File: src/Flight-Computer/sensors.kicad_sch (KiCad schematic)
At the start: 36 parts, among them P4 440054-3, P5 440054-3, P6 440054-3, P7 440054-3, Q1 QS5U17TR, Q2 QS5U17TR, Q3 QS5U17TR, Q4 QS5U17TR, U3 BMI323, U4 MAX-8C-0-10, U5 BMP390

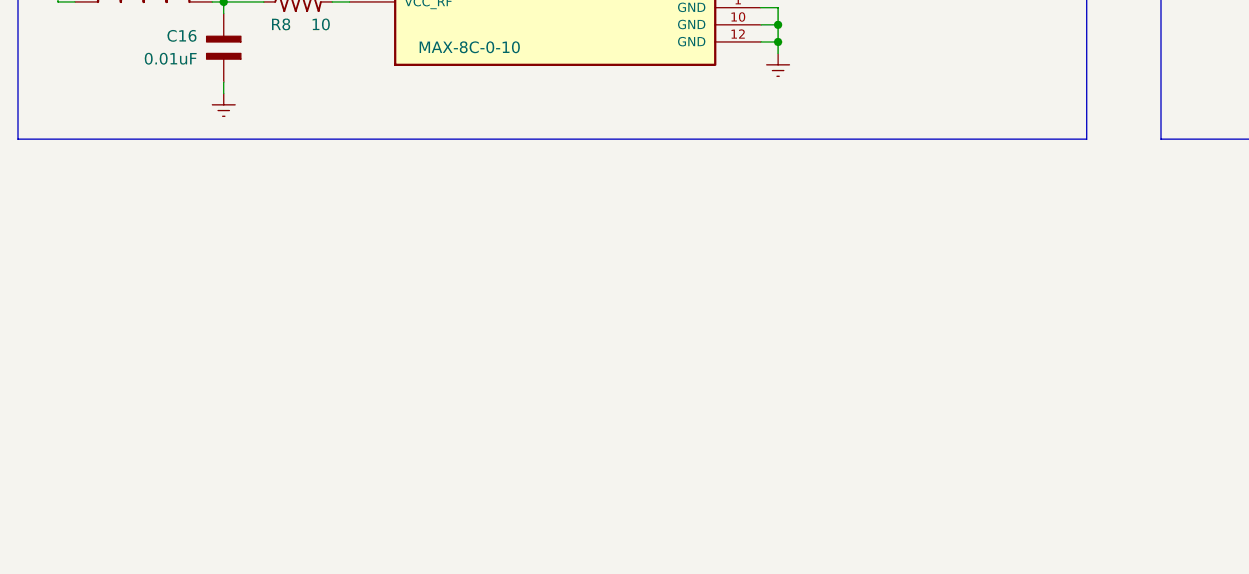
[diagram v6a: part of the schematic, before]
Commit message: implemented magnetometer in schematic
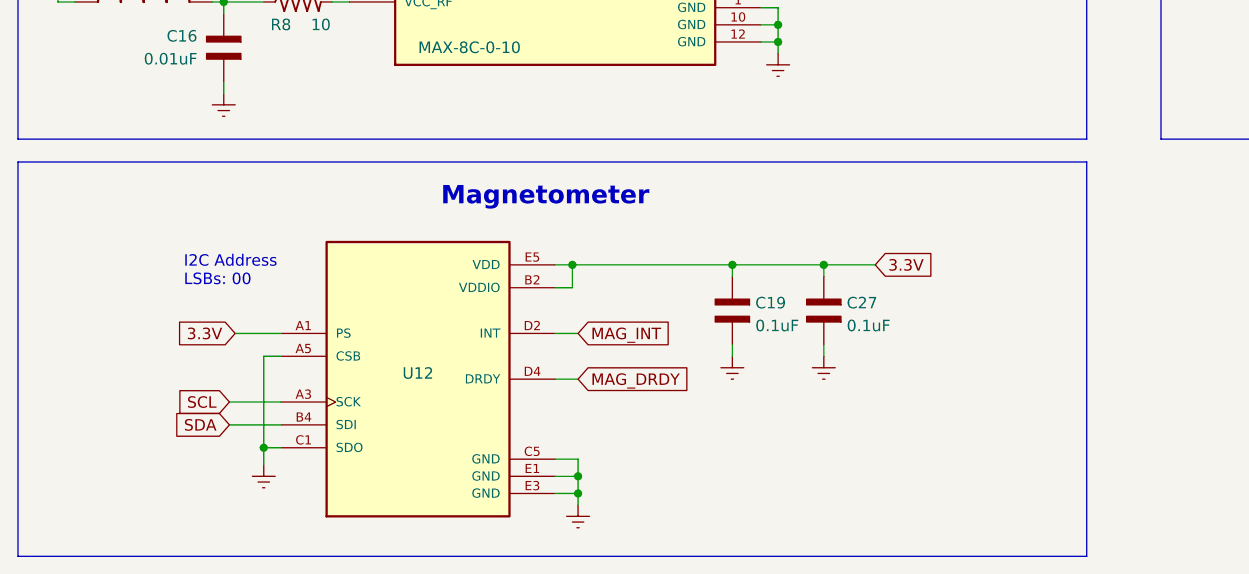
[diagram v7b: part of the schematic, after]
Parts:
- added C19, C27: 0.1uF, Flight-Computer:CAP_0603, symbol Flight-Computer:CAP_0603
- added U12: BMM150, Flight-Computer:BMM150, symbol Flight-Computer:BMM150
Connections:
- net 3.3V: now also C19.1, C27.1, U12.A1 (PS), U12.B2 (VDDIO), U12.E5 (VDD)
- net Earth: now also C19.2, C27.2, U12.A5 (CSB), U12.C1 (SDO), U12.C5 (GND), U12.E1 (GND), U12.E3 (GND)
- net SCL: now also U12.A3 (SCK)
- net SDA: now also U12.B4 (SDI)
- new net MAG_DRDY: U12.D4 (DRDY)
- new net MAG_INT: U12.D2 (INT)
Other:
- note added: "I2C Address LSBs: 00"
- note added: "Magnetometer"

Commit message: matched footprints to symbols
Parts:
- Q1, Q2, Q3, Q4: footprint Engine-Controller:QS5U17TR -> Flight-Computer:QS5U17TR
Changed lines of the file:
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@@
     (pin "1")
   )
-  (symbol (lib_name "QS5U17TR_1") (lib_id "Flight-Computer:QS5U17TR") (at 182.88 104.775 0) (unit 1)
+  (symbol (lib_id "Flight-Computer:QS5U17TR") (at 182.88 104.775 0) (unit 1)
     (in_bom yes) (on_board yes) (fields_autoplaced)
     (property "Reference" "Q1" (id 0) (at 188.087 105.2088 0)
@@
       (effects (font (size 1.27 1.27)) (justify left) hide)
     )
-    (property "Footprint" "Engine-Controller:QS5U17TR" (id 2) (at 184.785 120.65 0)
+    (property "Footprint" "Flight-Computer:QS5U17TR" (id 2) (at 184.785 120.65 0)
       (effects (font (size 1.27 1.27) italic) (justify left) hide)
     )
@@
       (effects (font (size 1.27 1.27)) (justify left) hide)
     )
-    (property "Footprint" "Engine-Controller:QS5U17TR" (id 2) (at 184.785 148.59 0)
+    (property "Footprint" "Flight-Computer:QS5U17TR" (id 2) (at 184.785 148.59 0)
       (effects (font (size 1.27 1.27) italic) (justify left) hide)
     )
@@
       (effects (font (size 1.27 1.27)) (justify left) hide)
     )
-    (property "Footprint" "Engine-Controller:QS5U17TR" (id 2) (at 241.3 120.015 0)
+    (property "Footprint" "Flight-Computer:QS5U17TR" (id 2) (at 241.3 120.015 0)
       (effects (font (size 1.27 1.27) italic) (justify left) hide)
     )
@@
       (effects (font (size 1.27 1.27)) (justify left) hide)
     )
-    (property "Footprint" "Engine-Controller:QS5U17TR" (id 2) (at 241.3 147.955 0)
+    (property "Footprint" "Flight-Computer:QS5U17TR" (id 2) (at 241.3 147.955 0)
       (effects (font (size 1.27 1.27) italic) (justify left) hide)
     )
